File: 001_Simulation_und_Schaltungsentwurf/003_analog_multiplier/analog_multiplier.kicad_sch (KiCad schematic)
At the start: 28 parts, among them IC1 MPY634KP, IC2 MPY634KP, IC3 MPY634KP, IC4 MPY634KP, U1 TL082, U2 TL082, U3 TL082

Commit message: Weiterarbeit Stand 20.10
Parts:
- added C7: {c}, symbol Device:C_Small
- added IC5: MPY634KP, DIP794W53P254L1930H508Q14N, symbol BA_Footprints:MPY634KP
- added R7, R8, R9: {R}, 000_Footprints:Resistor, symbol Device:R_Small
- added U4: TL082, Package_DIP:CERDIP-8_W7.62mm_SideBrazed_LongPads_Socket, symbol Amplifier_Operational:TL082
- added V10: 7.47, symbol Simulation_SPICE:VDC
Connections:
- net +10V: now also IC5.4 (SCALE_FACTOR)
- net +15V: now also IC5.14 (+VS), U4.8 (V+)
- net -15V: now also IC5.8 (-VS), U4.4 (V-)
- net GND: now also IC5.10 (Z_2_INPUT), IC5.2 (X_2_INPUT), IC5.7 (Y_2_INPUT), U4.3 (+), V10.2
- net detec_out180: now also R8.1
- net mult1_y: now also R7.1
- new net: R9.1, V10.1
- new net: C7.1, R7.2, U4.2 (-)
- new net mult_out_C: C7.2, IC5.11 (Z_1_INPUT), IC5.12 (OUTPUT)
- new net op_mult_in: IC5.1 (X_1_INPUT), R8.2, R9.2
- new net op_out: IC5.6 (Y_1_INPUT), U4.1
- no-connect marks 16 -> 20
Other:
- moved on the sheet: U3C

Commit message: Weiterarbeit Stand 24.10 (angepasste Dateigröße)
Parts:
- added C8, C9: {c}, symbol Device:C_Small
- added IC6, IC7: MPY634KP, DIP794W53P254L1930H508Q14N, symbol BA_Footprints:MPY634KP
- added R10, R11, R12, R13, R14, R15: {R}, 000_Footprints:Resistor, symbol Device:R_Small
- added unit 2 of U4
- added U5: TL082, Package_DIP:CERDIP-8_W7.62mm_SideBrazed_LongPads_Socket, symbol Amplifier_Operational:TL082
- added V11, V12: 15.75, symbol Simulation_SPICE:VDC
- V10: value 7.47 -> 15.75
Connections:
- net +10V: now also IC6.4 (SCALE_FACTOR), IC7.4 (SCALE_FACTOR)
- net +15V: now also IC6.14 (+VS), IC7.14 (+VS), U5.8 (V+)
- net -15V: now also IC6.8 (-VS), IC7.8 (-VS), U5.4 (V-)
- net GND: now also IC6.10 (Z_2_INPUT), IC6.2 (X_2_INPUT), IC6.7 (Y_2_INPUT), IC7.10 (Z_2_INPUT), IC7.2 (X_2_INPUT), IC7.7 (Y_2_INPUT), U4.5 (+), U5.3 (+), V11.2, V12.2
- net detec_out0: now also R8.1
- net detec_out180: now also R13.1; no longer R8.1
- net detec_out90: now also R10.1
- net mult1_y: now also R12.1, R15.1
- net mult_out_C renamed mult_out_C1
- net op_mult_in renamed op_mult_in1
- net op_out renamed VCI_out0
- new net: C8.1, R12.2, U4.6 (-)
- new net: C9.1, R15.2, U5.2 (-)
- new net: R14.1, V12.1
- new net: R11.1, V11.1
- new net VCI_out180: IC7.6 (Y_1_INPUT), U5.1
- new net VCI_out90: IC6.6 (Y_1_INPUT), U4.7
- new net mult_out_C2: C8.2, IC6.11 (Z_1_INPUT), IC6.12 (OUTPUT)
- new net mult_out_C3: C9.2, IC7.11 (Z_1_INPUT), IC7.12 (OUTPUT)
- new net op_mult_in2: IC6.1 (X_1_INPUT), R10.2, R11.2
- new net op_mult_in3: IC7.1 (X_1_INPUT), R13.2, R14.2
- no-connect marks 20 -> 28
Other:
- moved on the sheet: C7, IC5, R7, R8, R9, U1C, U2C, U3C, U4A, U4C, V10

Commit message: Stand 24.10
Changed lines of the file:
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@@
 		(stroke
 			(width 0)
-			(type default)
+			(type solid)
 		)
 		(fill
@@
 	)
 	(rectangle
-		(start 16.51 16.51)
-		(end 163.83 104.14)
+		(start 13.97 15.24)
+		(end 161.29 102.87)
 		(stroke
 			(width 0)

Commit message: documentation of the PCB (iteration 1)
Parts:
- removed V10, V11, V12: 15.75, symbol Simulation_SPICE:VDC
- added C4, C5: {c}, symbol Device:C_Small
- added IC4, IC5: MPY634KP, DIP794W53P254L1930H508Q14N, symbol BA_Footprints:MPY634KP
- added R4, R5: {R}, 000_Footprints:Resistor, symbol Device:R_Small
- added U3: TL082, Package_DIP:CERDIP-8_W7.62mm_SideBrazed_LongPads_Socket, symbol Amplifier_Operational:TL082
- added unit 2 of U4
- added V7, V8: VSIN, symbol Simulation_SPICE:VSIN
- renumbered C8 to C10, C9 to C11, C4 to C6, C5 to C7, C6 to C8, C7 to C9, IC4 to IC6, IC5 to IC7, IC6 to IC8, IC7 to IC9, R13 to R11, R9 to R12, R11 to R13, R7 to R15, R12 to R16, R15 to R17, R4 to R6, R5 to R7, R6 to R8, R8 to R9, U5 to U4, U3 to U5, U4 to U6, V8 to V10, V9 to V11, V7 to V9
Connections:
- net +10V: now also IC4.4 (SCALE_FACTOR), IC5.4 (SCALE_FACTOR)
- net +15V: now also IC4.14 (+VS), IC5.14 (+VS), U3.8 (V+)
- net -15V: now also IC4.8 (-VS), IC5.8 (-VS), U3.4 (V-)
- net GND: now also IC4.10 (Z_2_INPUT), IC4.2 (X_2_INPUT), IC4.7 (Y_2_INPUT), IC5.10 (Z_2_INPUT), IC5.2 (X_2_INPUT), IC5.7 (Y_2_INPUT), U3.3 (+), U4.5 (+), V7.2, V8.2
- net mult1_y: now also IC4.6 (Y_1_INPUT), IC5.6 (Y_1_INPUT)
- new net: C4.1, R4.2, U3.2 (-)
- new net: C5.1, R5.2, U4.6 (-)
- new net detec_out_mHz: C5.2, U4.7
- new net detec_out_pHz: C4.2, U3.1
- new net mHz: IC5.1 (X_1_INPUT), V7.1
- new net mult_out_mHz: IC5.11 (Z_1_INPUT), IC5.12 (OUTPUT), R5.1
- new net mult_out_pHz: IC4.11 (Z_1_INPUT), IC4.12 (OUTPUT), R4.1
- new net pHz: IC4.1 (X_1_INPUT), V8.1
- no-connect marks 28 -> 36
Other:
- note added: "Ergebnisse für Signale gleicher Frequenz mit Phasenverschiebung"
- moved on the sheet: C10, C11, C6, C7, C8, C9, IC6, IC7, IC8, IC9, R10, R11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

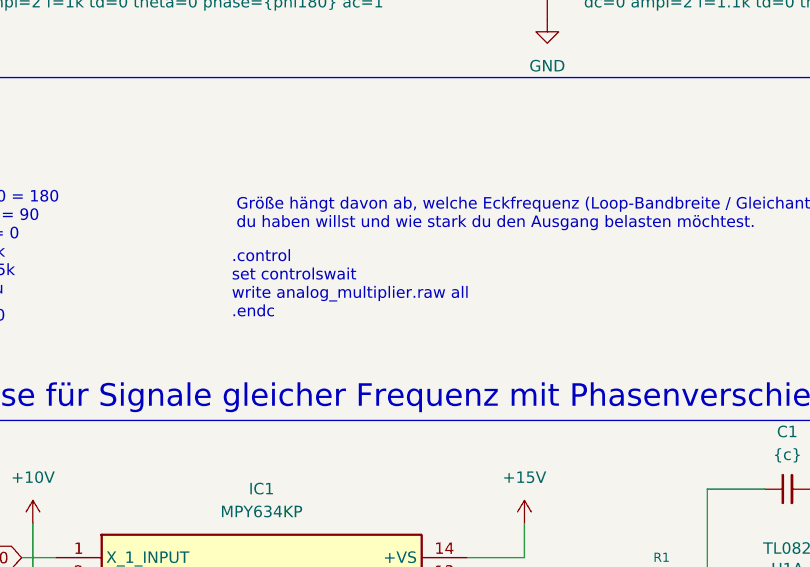
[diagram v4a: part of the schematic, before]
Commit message: LTspice sim added
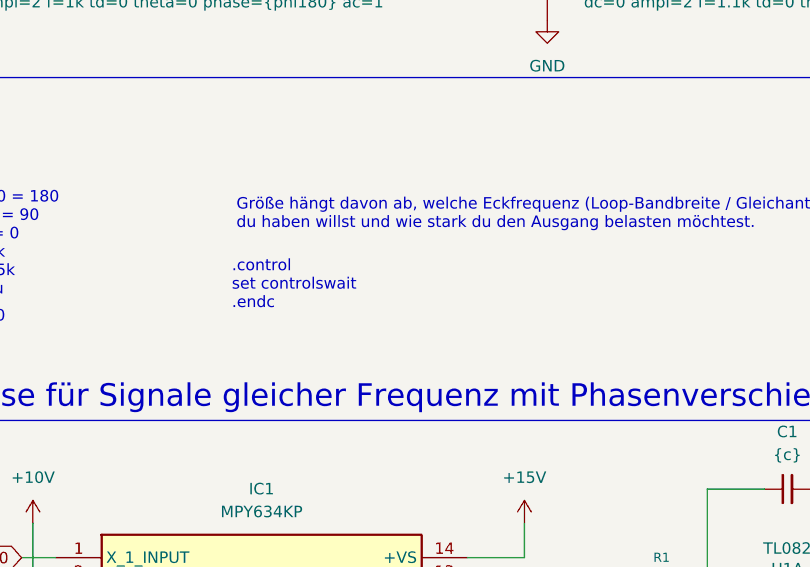
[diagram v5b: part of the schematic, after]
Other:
- note added: ".control set controlswait .endc"
- note removed: ".control set controlswait write analog_multiplier.raw all .endc"
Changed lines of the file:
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@@
 		)
 	)
-	(text ".control\nset controlswait\nwrite analog_multiplier.raw all\n.endc"
+	(text ".control\nset controlswait\n.endc"
 		(exclude_from_sim no)
 		(at 57.658 125.984 0)
